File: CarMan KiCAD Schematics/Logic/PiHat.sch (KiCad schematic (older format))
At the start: 11 parts, among them J7 Conn_01x02_Male, U2 ISO1050DUB, U8 MCP2515-xSO, Y1 16MHz

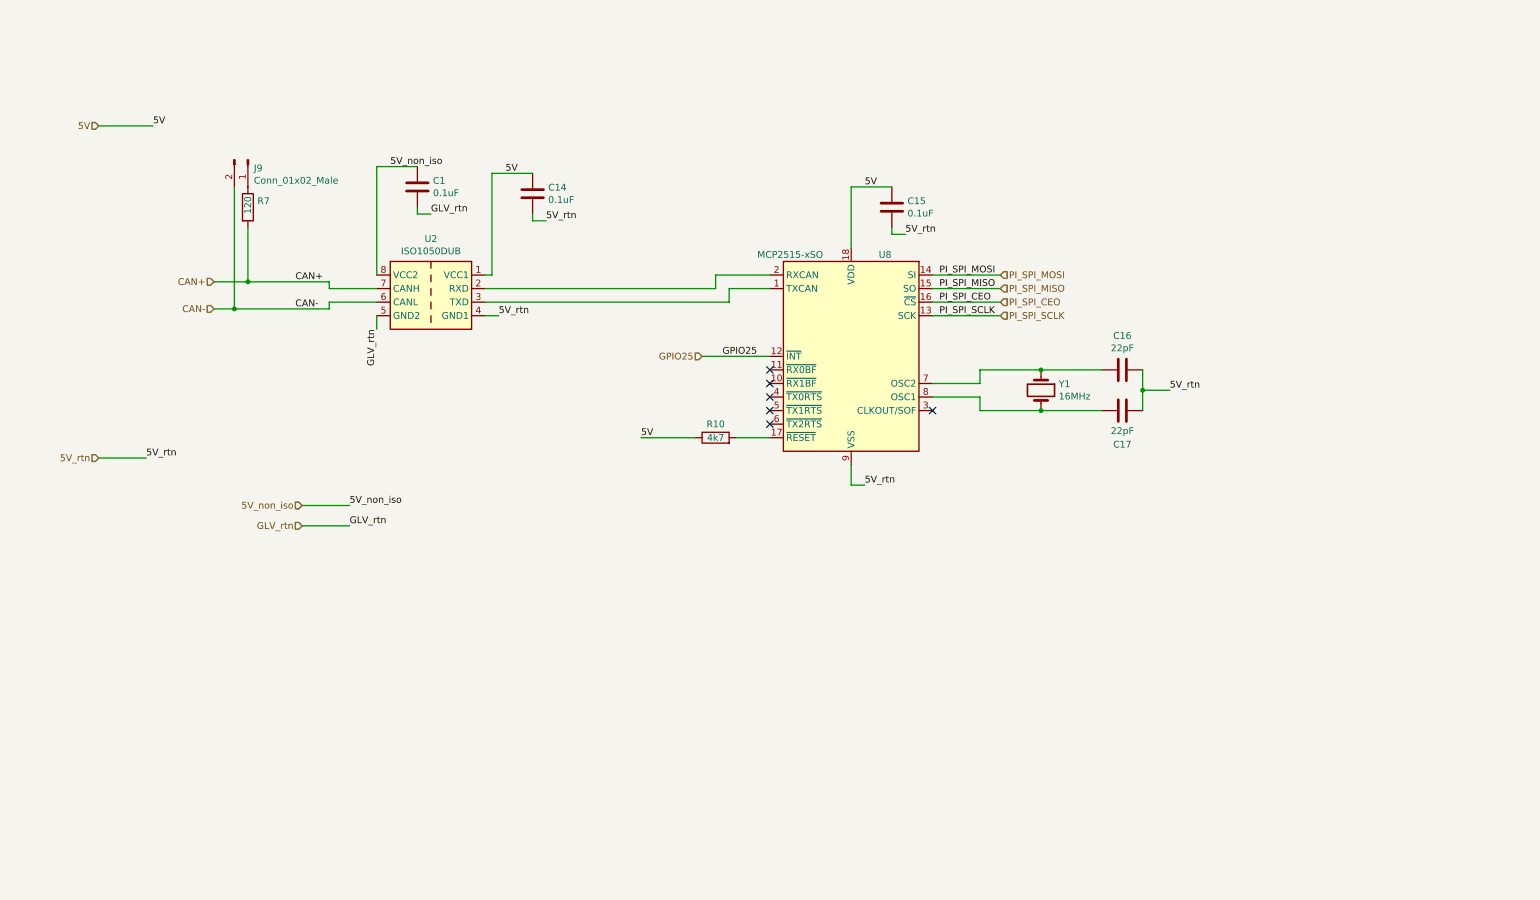
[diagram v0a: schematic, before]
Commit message: - limited shorting wires and clarified ISO connections - Removed 5V_rtn and 3.3V_rtn and changed to ISO_RTN - 3.3V designated as 3.3V_ISO - 5V designated as 5V_ISO
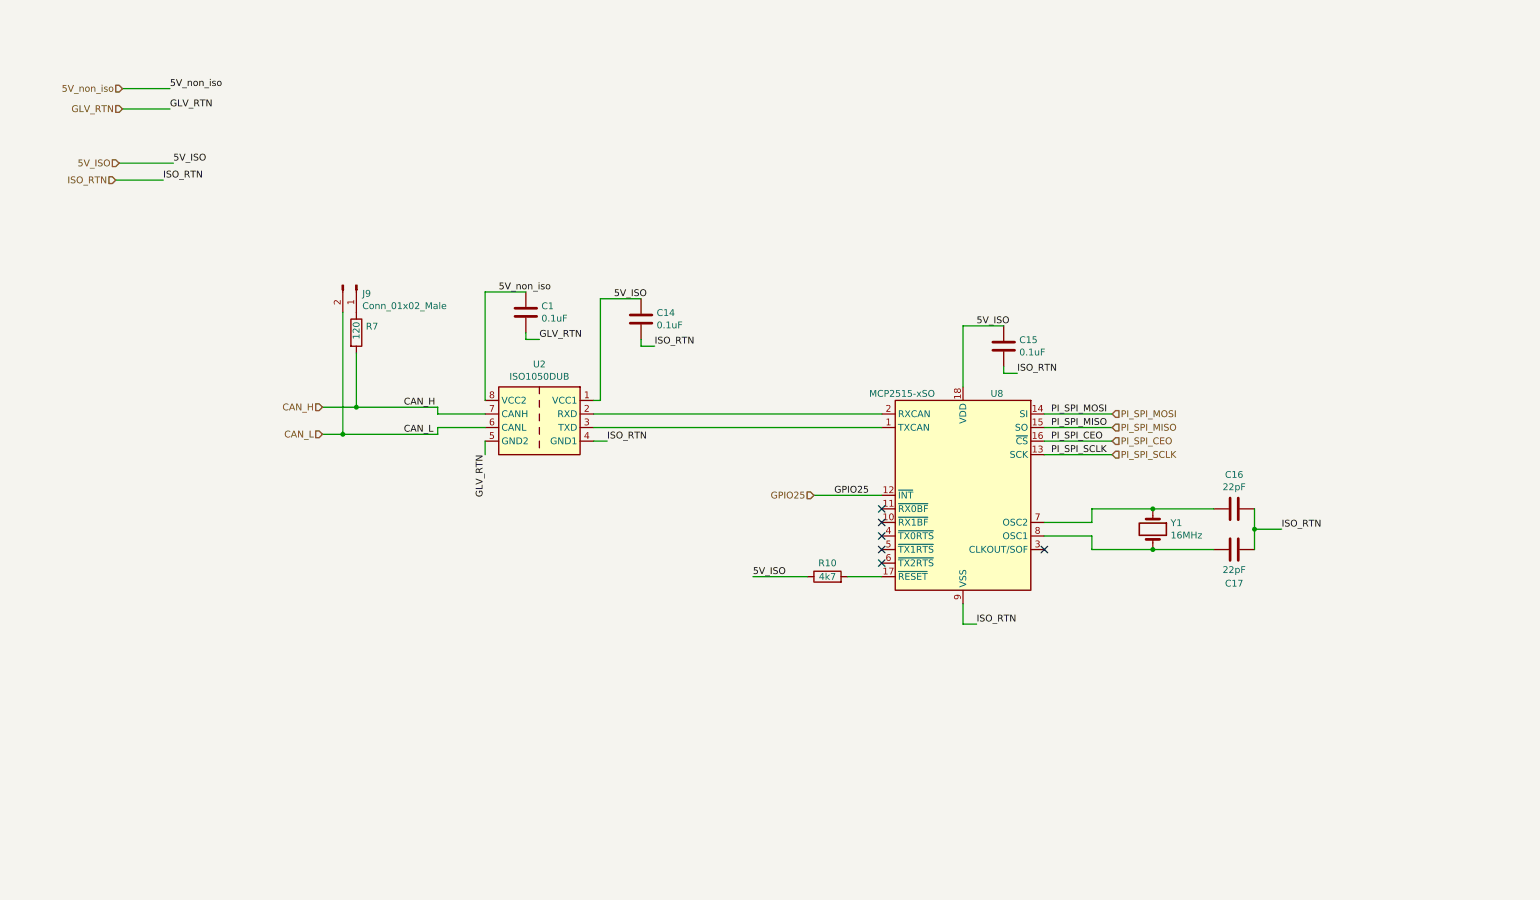
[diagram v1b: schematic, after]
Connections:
- net 5V renamed 5V_ISO
- net 5V_rtn renamed ISO_RTN
- net CAN+ renamed CAN_H
- net CAN- renamed CAN_L
- net GLV_rtn renamed GLV_RTN
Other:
- moved on the sheet: C1, C14, C15, C16, C17, J9, R10, R7, U2, U8, Y1

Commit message: Logic Further organization
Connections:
- net 5V_non_iso renamed 5V_NON_ISO
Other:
- note added: "ISO"
- note added: "NON-ISO"
- note added: "SIGNALS"
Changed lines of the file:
@@
 Comment4 ""
 $EndDescr
-Text HLabel 1350 1675 0    50   Input ~ 0
+Text HLabel 1300 1625 0    50   Input ~ 0
 5V_ISO
 $Comp
@@
 	-1   0    0    -1
 $EndComp
-Text HLabel 1325 1800 0    50   Input ~ 0
-ISO_RTN
-Text HLabel 2850 3675 0    50   Input ~ 0
+Text HLabel 1300 1725 0    50   Input ~ 0
+ISO_RTN
+Text Label 3450 3525 0    50   ~ 0
+CAN_H
+Text Label 3450 3625 0    50   ~ 0
 CAN_L
-Text HLabel 2850 3475 0    50   Input ~ 0
-CAN_H
-Wire Wire Line
-	2850 3475 3100 3475
-Wire Wire Line
-	2850 3675 3000 3675
-Wire Wire Line
-	1350 1675 1750 1675
-Wire Wire Line
-	1325 1800 1675 1800
-Text Label 3450 3475 0    50   ~ 0
-CAN_H
-Text Label 3450 3675 0    50   ~ 0
-CAN_L
-Text Label 1750 1675 0    50   ~ 0
-5V_ISO
-Text Label 1675 1800 0    50   ~ 0
+Text Label 2000 1625 2    50   ~ 0
+5V_ISO
+Text Label 2000 1725 2    50   ~ 0
 ISO_RTN
 $Comp
@@
 $EndComp
 Wire Wire Line
-	3100 3075 3100 3475
-Connection ~ 3100 3475
-Wire Wire Line
-	3100 3475 3700 3475
-Wire Wire Line
-	3000 2775 3000 3675
-Connection ~ 3000 3675
+	3000 2775 3000 3625
 Wire Wire Line
 	4900 2675 5200 2675
@@
 Text Label 5300 3025 0    50   ~ 0
 ISO_RTN
-Text Label 4950 3725 0    50   ~ 0
-ISO_RTN
-Wire Wire Line
-	4850 3725 4950 3725
+Text Label 5450 3725 2    50   ~ 0
+ISO_RTN
 NoConn ~ 8175 4525
 Text Label 7675 5075 0    50   ~ 0
@@
 Wire Wire Line
 	6975 4125 6475 4125
-Text Label 6625 4125 0    50   ~ 0
-GPIO25
-Text HLabel 6475 4125 0    50   Input ~ 0
+Text Label 6475 4125 0    50   ~ 0
 GPIO25
 NoConn ~ 6975 4225
@@
 Text Label 6025 4725 0    50   ~ 0
 5V_ISO
-Wire Wire Line
-	8175 3525 8675 3525
-Wire Wire Line
-	8175 3625 8675 3625
-Wire Wire Line
-	8175 3725 8675 3725
-Wire Wire Line
-	8175 3825 8675 3825
-Text Label 8225 3525 0    50   ~ 0
+Text Label 8825 3525 2    50   ~ 0
 PI_SPI_MOSI
-Text Label 8225 3625 0    50   ~ 0
+Text Label 8825 3625 2    50   ~ 0
 PI_SPI_MISO
-Text Label 8225 3725 0    50   ~ 0
+Text Label 8825 3725 2    50   ~ 0
 PI_SPI_CEO
-Text Label 8225 3825 0    50   ~ 0
+Text Label 8825 3825 2    50   ~ 0
 PI_SPI_SCLK
 $Comp
@@
 Text Label 9925 4375 0    50   ~ 0
 ISO_RTN
-Text HLabel 8675 3525 2    50   Input ~ 0
-PI_SPI_MOSI
-Text HLabel 8675 3625 2    50   Input ~ 0
-PI_SPI_MISO
-Text HLabel 8675 3725 2    50   Input ~ 0
-PI_SPI_CEO
-Text HLabel 8675 3825 2    50   Input ~ 0
-PI_SPI_SCLK
-$Comp
-L Logic-rescue:ISO1050DUB-Interface_CAN_LIN-Logic-rescue U2
-U 1 1 5FAD2713
-P 4450 3525
-F 0 "U2" H 4450 3892 50  0000 C CNN
-F 1 "ISO1050DUB" H 4450 3801 50  0000 C CNN
-F 2 "Package_SO:SOP-8_6.62x9.15mm_P2.54mm" H 4450 3175 50  0001 C CIN
-F 3 "http://www.ti.com/lit/ds/symlink/iso1050.pdf" H 4450 3475 50  0001 C CNN
-	1    4450 3525
-	-1   0    0    -1
-$EndComp
 Wire Wire Line
 	4900 3425 4850 3425
@@
 	4350 2975 4450 2975
 Text Label 4150 2625 0    50   ~ 0
-5V_non_iso
+5V_NON_ISO
 Text Label 4450 2975 0    50   ~ 0
 GLV_RTN
-Text HLabel 1375 1125 0    50   Input ~ 0
-5V_non_iso
-Wire Wire Line
-	1375 1125 1725 1125
-Text Label 1725 1125 0    50   ~ 0
-5V_non_iso
-Wire Wire Line
-	3000 3675 3700 3675
-Wire Wire Line
-	4050 3525 3700 3525
-Wire Wire Line
-	3700 3525 3700 3475
-Wire Wire Line
-	3700 3675 3700 3625
-Wire Wire Line
-	3700 3625 4050 3625
+Text HLabel 1275 975  0    50   Input ~ 0
+5V_NON_ISO
+Text Label 1975 975  2    50   ~ 0
+5V_NON_ISO
 Wire Wire Line
 	4050 2625 4050 3425
-Text HLabel 1375 1275 0    50   Input ~ 0
+Text HLabel 1275 1075 0    50   Input ~ 0
 GLV_RTN
-Wire Wire Line
-	1375 1275 1725 1275
-Text Label 1725 1275 0    50   ~ 0
+Text Label 1975 1075 2    50   ~ 0
 GLV_RTN
-Text Label 4050 3825 3    50   ~ 0
+Text Label 3450 3725 0    50   ~ 0
 GLV_RTN
 Wire Wire Line
-	4050 3725 4050 3825
-Wire Wire Line
 	6975 3525 4850 3525
 Wire Wire Line
 	4850 3625 6975 3625
+Text Notes 1200 700  0    79   ~ 0
+SIGNALS
+Wire Notes Line
+	2350 550  550  550
+Wire Wire Line
+	1275 975  1975 975
+Wire Wire Line
+	1275 1075 1975 1075
+Wire Wire Line
+	3000 3625 4050 3625
+Wire Wire Line
+	3100 3075 3100 3525
+Wire Wire Line
+	3100 3525 4050 3525
+Wire Wire Line
+	3450 3725 4050 3725
+$Comp
+L Logic-rescue:ISO1050DUB-Interface_CAN_LIN-Logic-rescue U2
+U 1 1 5FAD2713
+P 4450 3525
+F 0 "U2" H 4450 3892 50  0000 C CNN
+F 1 "ISO1050DUB" H 4450 3801 50  0000 C CNN
+F 2 "Package_SO:SOP-8_6.62x9.15mm_P2.54mm" H 4450 3175 50  0001 C CIN
+F 3 "http://www.ti.com/lit/ds/symlink/iso1050.pdf" H 4450 3475 50  0001 C CNN
+	1    4450 3525
+	-1   0    0    -1
+$EndComp
+Wire Wire Line
+	4850 3725 5450 3725
+Wire Wire Line
+	1300 1625 2000 1625
+Wire Wire Line
+	1300 1725 2000 1725
+Text Label 1975 1175 2    50   ~ 0
+CAN_H
+Text Label 1975 1275 2    50   ~ 0
+CAN_L
+Wire Wire Line
+	1275 1175 1975 1175
+Wire Wire Line
+	1275 1275 1975 1275
+Text HLabel 1275 1275 0    50   Input ~ 0
+CAN_L
+Text HLabel 1275 1175 0    50   Input ~ 0
+CAN_H
+Wire Notes Line
+	550  1375 2350 1375
+Text Notes 625  875  0    59   ~ 0
+NON-ISO
+Wire Notes Line
+	2350 750  550  750
+Text Notes 625  1525 0    59   ~ 0
+ISO
+Text Label 2000 1825 2    50   ~ 0
+GPIO25
+Text HLabel 1300 1825 0    50   Output ~ 0
+GPIO25
+Wire Wire Line
+	1300 1825 2000 1825
+Text Label 2000 2225 2    50   ~ 0
+PI_SPI_MOSI
+Text Label 2000 2125 2    50   ~ 0
+PI_SPI_MISO
+Text Label 2000 2025 2    50   ~ 0
+PI_SPI_CEO
+Text Label 2000 1925 2    50   ~ 0
+PI_SPI_SCLK
+Text HLabel 1300 2225 0    50   Output ~ 0
+PI_SPI_MOSI
+Text HLabel 1300 2125 0    50   Output ~ 0
+PI_SPI_MISO
+Text HLabel 1300 2025 0    50   Output ~ 0
+PI_SPI_CEO
+Text HLabel 1300 1925 0    50   Output ~ 0
+PI_SPI_SCLK
+Wire Wire Line
+	1300 1925 2000 1925
+Wire Wire Line
+	1300 2025 2000 2025
+Wire Wire Line
+	1300 2125 2000 2125
+Wire Wire Line
+	1300 2225 2000 2225
+Wire Wire Line
+	8175 3525 8825 3525
+Wire Wire Line
+	8175 3625 8825 3625
+Wire Wire Line
+	8175 3725 8825 3725
+Wire Wire Line
+	8175 3825 8825 3825
+Wire Notes Line
+	2350 2375 550  2375
+Wire Notes Line
+	550  550  550  2375
+Wire Notes Line
+	2350 550  2350 2375
 $EndSCHEMATC

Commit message: Super organized logic
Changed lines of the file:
@@
 Text Label 2000 1925 2    50   ~ 0
 PI_SPI_SCLK
-Text HLabel 1300 2225 0    50   Output ~ 0
+Text HLabel 1300 2225 0    50   Input ~ 0
 PI_SPI_MOSI
 Text HLabel 1300 2125 0    50   Output ~ 0

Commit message: Logic Update
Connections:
- net 5V_ISO: now also C14.2; no longer C14.1
- net 5V_NON_ISO: now also C1.2; no longer C1.1
- net GLV_RTN: now also C1.1; no longer C1.2
- net ISO_RTN: now also C14.1; no longer C14.2
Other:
- note added: "CAN Controller with SPI Interface"
- note added: "Isolated Can Transceiver"
- note added: "PiHat & CAN Transceiver"
- moved on the sheet: C1, C14, C15, J9, R10, R7
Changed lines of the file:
@@
 Text HLabel 1300 1625 0    50   Input ~ 0
 5V_ISO
-$Comp
-L Logic-rescue:MCP2515-xSO-Interface_CAN_LIN-Logic-rescue U8
-U 1 1 5F9A99EE
-P 7575 4125
-F 0 "U8" H 7325 4875 50  0000 C CNN
-F 1 "MCP2515-xSO" H 8025 4875 50  0000 C CNN
-F 2 "Package_SO:SOIC-18W_7.5x11.6mm_P1.27mm" H 7575 3225 50  0001 C CIN
-F 3 "http://ww1.microchip.com/downloads/en/DeviceDoc/21801e.pdf" H 7675 3325 50  0001 C CNN
-	1    7575 4125
-	-1   0    0    -1
-$EndComp
 Text HLabel 1300 1725 0    50   Input ~ 0
 ISO_RTN
-Text Label 3450 3525 0    50   ~ 0
+Text Label 3475 3525 0    50   ~ 0
 CAN_H
-Text Label 3450 3625 0    50   ~ 0
+Text Label 3475 3625 0    50   ~ 0
 CAN_L
 Text Label 2000 1625 2    50   ~ 0
@@
 L Logic-rescue:Conn_01x02_Male-Connector-Logic-rescue J7
 U 1 1 5F9AE3B8
-P 3100 2575
+P 2850 2575
 AR Path="/5F9AE3B8" Ref="J7"  Part="1"
 AR Path="/5F9A7CF0/5F9AE3B8" Ref="J9"  Part="1"
-F 0 "J9" V 3162 2619 50  0000 L CNN
-F 1 "Conn_01x02_Male" V 3253 2619 50  0000 L CNN
-F 2 "Connector_PinSocket_2.54mm:PinSocket_1x02_P2.54mm_Vertical" H 3100 2575 50  0001 C CNN
-F 3 "~" H 3100 2575 50  0001 C CNN
-	1    3100 2575
+F 0 "J9" V 2912 2619 50  0000 L CNN
+F 1 "Conn_01x02_Male" V 3050 1725 50  0001 L CNN
+F 2 "Connector_PinSocket_2.54mm:PinSocket_1x02_P2.54mm_Vertical" H 2850 2575 50  0001 C CNN
+F 3 "~" H 2850 2575 50  0001 C CNN
+	1    2850 2575
 	0    1    1    0
 $EndComp
@@
 L Logic-rescue:R-Device-Logic-rescue R7
 U 1 1 5F9AF7D2
-P 3100 2925
+P 2850 2925
 AR Path="/5F9AF7D2" Ref="R7"  Part="1"
 AR Path="/5F9A7CF0/5F9AF7D2" Ref="R7"  Part="1"
-F 0 "R7" H 3170 2971 50  0000 L CNN
-F 1 "120" V 3100 2875 50  0000 L CNN
-F 2 "Resistor_SMD:R_0805_2012Metric_Pad1.15x1.40mm_HandSolder" V 3030 2925 50  0001 C CNN
-F 3 "~" H 3100 2925 50  0001 C CNN
-	1    3100 2925
+F 0 "R7" H 2920 2971 50  0000 L CNN
+F 1 "120" V 2850 2875 50  0000 L CNN
+F 2 "Resistor_SMD:R_0805_2012Metric_Pad1.15x1.40mm_HandSolder" V 2780 2925 50  0001 C CNN
+F 3 "~" H 2850 2925 50  0001 C CNN
+	1    2850 2925
 	1    0    0    -1
 $EndComp
 Wire Wire Line
-	3000 2775 3000 3625
-Wire Wire Line
-	4900 2675 5200 2675
-$Comp
-L Logic-rescue:C-Device-Logic-rescue C14
-U 1 1 5F9B08F3
-P 5200 2825
-AR Path="/5F9B08F3" Ref="C14"  Part="1"
-AR Path="/5F9A7CF0/5F9B08F3" Ref="C14"  Part="1"
-F 0 "C14" H 5315 2871 50  0000 L CNN
-F 1 "0.1uF" H 5315 2780 50  0000 L CNN
-F 2 "Capacitor_SMD:C_0805_2012Metric_Pad1.15x1.40mm_HandSolder" H 5238 2675 50  0001 C CNN
-F 3 "~" H 5200 2825 50  0001 C CNN
-	1    5200 2825
-	1    0    0    -1
-$EndComp
-Wire Wire Line
-	5200 2975 5200 3025
-Wire Wire Line
-	5200 3025 5300 3025
-Text Label 5000 2675 0    50   ~ 0
-5V_ISO
-Text Label 5300 3025 0    50   ~ 0
-ISO_RTN
-Text Label 5450 3725 2    50   ~ 0
+	2750 2775 2750 3625
+Wire Wire Line
+	5425 3375 5425 3425
+Text Label 5075 3025 0    50   ~ 0
+ISO_RTN
+Text Label 5425 3725 2    50   ~ 0
 ISO_RTN
 NoConn ~ 8175 4525
-Text Label 7675 5075 0    50   ~ 0
-ISO_RTN
-Wire Wire Line
-	7575 4925 7575 5075
-Wire Wire Line
-	7575 5075 7675 5075
-Wire Wire Line
-	7575 3325 7575 2875
-Wire Wire Line
-	7575 2875 7875 2875
+Text Label 8000 5250 2    50   ~ 0
+ISO_RTN
+Wire Wire Line
+	7575 3000 7875 3000
 $Comp
 L Logic-rescue:C-Device-Logic-rescue C15
 U 1 1 5F9BD77C
-P 7875 3025
+P 8025 3000
 AR Path="/5F9BD77C" Ref="C15"  Part="1"
 AR Path="/5F9A7CF0/5F9BD77C" Ref="C15"  Part="1"
-F 0 "C15" H 7990 3071 50  0000 L CNN
-F 1 "0.1uF" H 7990 2980 50  0000 L CNN
-F 2 "Capacitor_SMD:C_0805_2012Metric_Pad1.15x1.40mm_HandSolder" H 7913 2875 50  0001 C CNN
-F 3 "~" H 7875 3025 50  0001 C CNN
-	1    7875 3025
-	1    0    0    -1
-$EndComp
-Wire Wire Line
-	7875 3175 7875 3225
-Wire Wire Line
-	7875 3225 7975 3225
-Text Label 7675 2875 0    50   ~ 0
-5V_ISO
-Text Label 7975 3225 0    50   ~ 0
-ISO_RTN
-Wire Wire Line
-	6975 4125 6475 4125
-Text Label 6475 4125 0    50   ~ 0
+F 0 "C15" V 8150 2925 50  0000 L CNN
+F 1 "0.1uF" V 7900 2900 50  0000 L CNN
+F 2 "Capacitor_SMD:C_0805_2012Metric_Pad1.15x1.40mm_HandSolder" H 8063 2850 50  0001 C CNN
+F 3 "~" H 8025 3000 50  0001 C CNN
+	1    8025 3000
+	0    -1   -1   0
+$EndComp
+Text Label 7575 3000 0    50   ~ 0
+5V_ISO
+Text Label 8475 3000 2    50   ~ 0
+ISO_RTN
+Text Label 6250 4125 0    50   ~ 0
 GPIO25
 NoConn ~ 6975 4225
@@
 L Logic-rescue:R-Device-Logic-rescue R10
 U 1 1 5F9C01C9
-P 6575 4725
+P 6725 4725
 AR Path="/5F9C01C9" Ref="R10"  Part="1"
 AR Path="/5F9A7CF0/5F9C01C9" Ref="R10"  Part="1"
-F 0 "R10" V 6675 4725 50  0000 C CNN
-F 1 "4k7" V 6575 4725 50  0000 C CNN
-F 2 "Resistor_SMD:R_0805_2012Metric_Pad1.15x1.40mm_HandSolder" V 6505 4725 50  0001 C CNN
-F 3 "~" H 6575 4725 50  0001 C CNN
-	1    6575 4725
+F 0 "R10" V 6825 4725 50  0000 C CNN
+F 1 "4k7" V 6725 4725 50  0000 C CNN
+F 2 "Resistor_SMD:R_0805_2012Metric_Pad1.15x1.40mm_HandSolder" V 6655 4725 50  0001 C CNN
+F 3 "~" H 6725 4725 50  0001 C CNN
+	1    6725 4725
 	0    -1   -1   0
 $EndComp
-Wire Wire Line
-	6725 4725 6975 4725
-Wire Wire Line
-	6425 4725 6025 4725
-Text Label 6025 4725 0    50   ~ 0
+Text Label 6250 4725 0    50   ~ 0
 5V_ISO
 Text Label 8825 3525 2    50   ~ 0
@@
 Wire Wire Line
 	9725 4225 9725 4375
-Wire Wire Line
-	9725 4375 9925 4375
 Connection ~ 9725 4375
 Wire Wire Line
 	9725 4375 9725 4525
-Text Label 9925 4375 0    50   ~ 0
-ISO_RTN
-Wire Wire Line
-	4900 3425 4850 3425
-Wire Wire Line
-	4900 2675 4900 3425
-Wire Wire Line
-	4050 2625 4350 2625
-$Comp
-L Logic-rescue:C-Device-Logic-rescue C1
-U 1 1 5FADAB07
-P 4350 2775
-AR Path="/5FADAB07" Ref="C1"  Part="1"
-AR Path="/5F9A7CF0/5FADAB07" Ref="C1"  Part="1"
-F 0 "C1" H 4465 2821 50  0000 L CNN
-F 1 "0.1uF" H 4465 2730 50  0000 L CNN
-F 2 "Capacitor_SMD:C_0805_2012Metric_Pad1.15x1.40mm_HandSolder" H 4388 2625 50  0001 C CNN
-F 3 "~" H 4350 2775 50  0001 C CNN
-	1    4350 2775
-	1    0    0    -1
-$EndComp
-Wire Wire Line
-	4350 2925 4350 2975
-Wire Wire Line
-	4350 2975 4450 2975
-Text Label 4150 2625 0    50   ~ 0
-5V_NON_ISO
-Text Label 4450 2975 0    50   ~ 0
+Text Label 10125 4375 2    50   ~ 0
+ISO_RTN
+Text Label 3825 3025 2    50   ~ 0
 GLV_RTN
 Text HLabel 1275 975  0    50   Input ~ 0
@@
 Text Label 1975 975  2    50   ~ 0
 5V_NON_ISO
-Wire Wire Line
-	4050 2625 4050 3425
 Text HLabel 1275 1075 0    50   Input ~ 0
 GLV_RTN
 Text Label 1975 1075 2    50   ~ 0
 GLV_RTN
-Text Label 3450 3725 0    50   ~ 0
+Text Label 3475 3725 0    50   ~ 0
 GLV_RTN
 Wire Wire Line
@@
 	1275 1075 1975 1075
 Wire Wire Line
-	3000 3625 4050 3625
-Wire Wire Line
-	3100 3075 3100 3525
-Wire Wire Line
-	3100 3525 4050 3525
-Wire Wire Line
-	3450 3725 4050 3725
+	2850 3075 2850 3525
 $Comp
 L Logic-rescue:ISO1050DUB-Interface_CAN_LIN-Logic-rescue U2
 U 1 1 5FAD2713
 P 4450 3525
-F 0 "U2" H 4450 3892 50  0000 C CNN
-F 1 "ISO1050DUB" H 4450 3801 50  0000 C CNN
+F 0 "U2" H 4450 3775 50  0000 C CNN
+F 1 "ISO1050DUB" H 4450 3175 50  0000 C CNN
 F 2 "Package_SO:SOP-8_6.62x9.15mm_P2.54mm" H 4450 3175 50  0001 C CIN
 F 3 "http://www.ti.com/lit/ds/symlink/iso1050.pdf" H 4450 3475 50  0001 C CNN
@@
 	-1   0    0    -1
 $EndComp
-Wire Wire Line
-	4850 3725 5450 3725
 Wire Wire Line
 	1300 1625 2000 1625
@@
 Wire Notes Line
 	2350 550  2350 2375
+Text Notes 7300 6950 0    197  ~ 0
+PiHat & CAN Transceiver
+Text Notes 3800 2775 0    79   ~ 0
+Isolated Can Transceiver
+Wire Wire Line
+	4850 3425 5425 3425
+Wire Wire Line
+	5425 3025 5425 3075
+Text Label 5375 3425 2    50   ~ 0
+5V_ISO
+Wire Wire Line
+	2850 3525 4050 3525
+Wire Wire Line
+	2750 3625 4050 3625
+Wire Wire Line
+	3475 3425 4050 3425
+Text Label 3475 3425 0    50   ~ 0
+5V_NON_ISO
+$Comp
+L Logic-rescue:C-Device-Logic-rescue C1
+U 1 1 5FADAB07
+P 3475 3225
+AR Path="/5FADAB07" Ref="C1"  Part="1"
+AR Path="/5F9A7CF0/5FADAB07" Ref="C1"  Part="1"
+F 0 "C1" H 3590 3271 50  0000 L CNN
+F 1 "0.1uF" H 3590 3180 50  0000 L CNN
+F 2 "Capacitor_SMD:C_0805_2012Metric_Pad1.15x1.40mm_HandSolder" H 3513 3075 50  0001 C CNN
+F 3 "~" H 3475 3225 50  0001 C CNN
+	1    3475 3225
+	1    0    0    -1
+$EndComp
+Wire Wire Line
+	3475 3375 3475 3425
+Wire Wire Line
+	3475 3025 3475 3075
+$Comp
+L Logic-rescue:C-Device-Logic-rescue C14
+U 1 1 5F9B08F3
+P 5425 3225
+AR Path="/5F9B08F3" Ref="C14"  Part="1"
+AR Path="/5F9A7CF0/5F9B08F3" Ref="C14"  Part="1"
+F 0 "C14" H 5540 3271 50  0000 L CNN
+F 1 "0.1uF" H 5540 3180 50  0000 L CNN
+F 2 "Capacitor_SMD:C_0805_2012Metric_Pad1.15x1.40mm_HandSolder" H 5463 3075 50  0001 C CNN
+F 3 "~" H 5425 3225 50  0001 C CNN
+	1    5425 3225
+	1    0    0    -1
+$EndComp
+Wire Wire Line
+	5075 3025 5425 3025
+Wire Wire Line
+	3475 3025 3825 3025
+Wire Wire Line
+	3475 3725 4050 3725
+Wire Wire Line
+	4850 3725 5425 3725
+Wire Notes Line
+	3250 3975 5800 3975
+Wire Wire Line
+	8175 3000 8475 3000
+$Comp
+L Logic-rescue:MCP2515-xSO-Interface_CAN_LIN-Logic-rescue U8
+U 1 1 5F9A99EE
+P 7575 4125
+F 0 "U8" H 7325 4875 50  0000 C CNN
+F 1 "MCP2515-xSO" H 7575 4275 50  0000 C CNN
+F 2 "Package_SO:SOIC-18W_7.5x11.6mm_P1.27mm" H 7575 3225 50  0001 C CIN
+F 3 "http://ww1.microchip.com/downloads/en/DeviceDoc/21801e.pdf" H 7675 3325 50  0001 C CNN
+	1    7575 4125
+	-1   0    0    -1
+$EndComp
+Wire Wire Line
+	7575 5250 8000 5250
+Wire Wire Line
+	7575 4925 7575 5250
+Wire Wire Line
+	7575 3000 7575 3325
+Wire Wire Line
+	6975 4725 6875 4725
+Wire Wire Line
+	6250 4725 6575 4725
+Wire Wire Line
+	6250 4125 6975 4125
+Wire Wire Line
+	9725 4375 10125 4375
+Wire Notes Line
+	6175 5375 10275 5375
+Wire Notes Line
+	10275 5375 10275 2500
+Wire Notes Line
+	10275 2500 6175 2500
+Wire Notes Line
+	6175 2500 6175 5375
+Text Notes 7275 2700 0    79   ~ 0
+CAN Controller with SPI Interface
+Wire Notes Line
+	5800 2500 5800 3975
+Wire Notes Line
+	3250 2500 5800 2500
+Wire Notes Line
+	3250 2500 3250 3975
 $EndSCHEMATC
